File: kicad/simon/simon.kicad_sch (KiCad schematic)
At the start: 20 parts, among them J1 GPIO, J2 Power, U1 74LS06

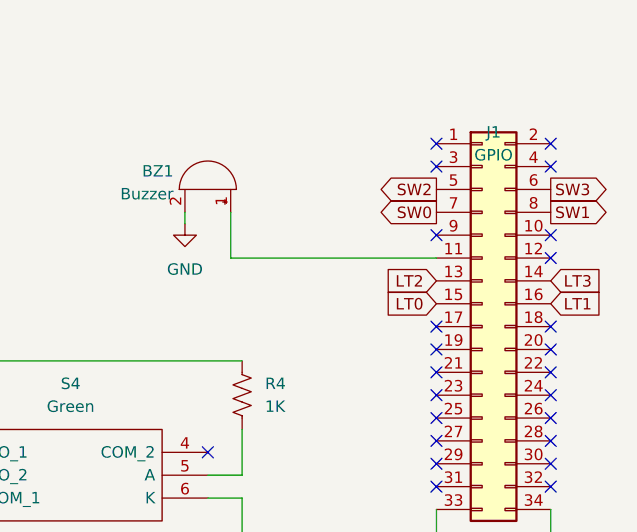
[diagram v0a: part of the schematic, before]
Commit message: Fixed trace routing to speaker.  This is the real production version.
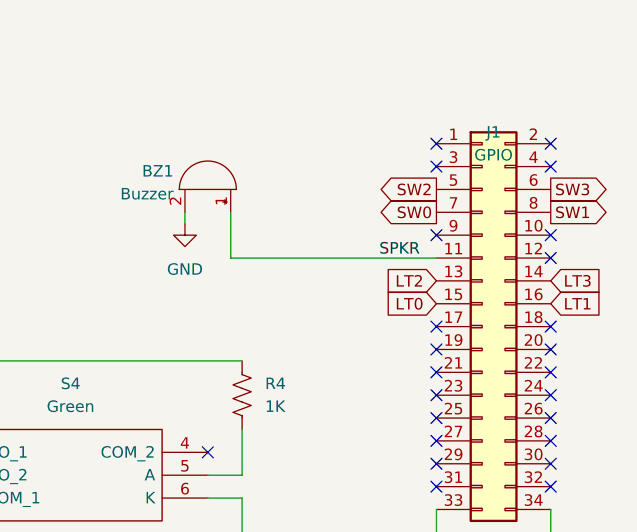
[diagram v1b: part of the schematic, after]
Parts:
- BZ1: footprint Buzzer_Beeper:Speaker_CUI_CMR-1206S-67 -> parts:XDCR_AT-1438-TWT-R
- S1, S2, S3, S4: footprint B3W9002Y1Y -> parts:B3W9002Y1Y
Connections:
- net SPKR: now reaches BZ1.1 (-), J1.11 (Pin_11)
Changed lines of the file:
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@@
     (stroke (width 0) (type default))
+  )
+  (label "SPKR" (at 201.93 46.99 0) (fields_autoplaced)
+    (effects (font (size 1.27 1.27)) (justify left bottom))
   )
   (global_label "LT0" (shape output) (at 49.53 95.25 180) (fields_autoplaced)
@@
       (effects (font (size 1.27 1.27)))
     )
-    (property "Footprint" "B3W9002Y1Y" (at 179.07 66.04 0)
+    (property "Footprint" "parts:B3W9002Y1Y" (at 179.07 66.04 0)
       (effects (font (size 1.27 1.27)) (justify left) hide)
     )
@@
       (effects (font (size 1.27 1.27)))
     )
-    (property "Footprint" "B3W9002Y1Y" (at 134.62 66.04 0)
+    (property "Footprint" "parts:B3W9002Y1Y" (at 134.62 66.04 0)
       (effects (font (size 1.27 1.27)) (justify left) hide)
     )
@@
       (effects (font (size 1.27 1.27)))
     )
-    (property "Footprint" "B3W9002Y1Y" (at 46.99 66.04 0)
+    (property "Footprint" "parts:B3W9002Y1Y" (at 46.99 66.04 0)
       (effects (font (size 1.27 1.27)) (justify left) hide)
     )
@@
       (effects (font (size 1.27 1.27)) (justify right))
     )
-    (property "Footprint" "Buzzer_Beeper:Speaker_CUI_CMR-1206S-67" (at 185.42 40.005 90)
+    (property "Footprint" "parts:XDCR_AT-1438-TWT-R" (at 185.42 40.005 90)
       (effects (font (size 1.27 1.27)) hide)
     )
@@
       (effects (font (size 1.27 1.27)))
     )
-    (property "Footprint" "B3W9002Y1Y" (at 91.44 66.04 0)
-      (effects (font (size 1.27 1.27)) (justify left) hide)
-    )
+    (property "Footprint" "parts:B3W9002Y1Y" (at 91.44 66.04 0)
+      (effects (font (size 1.27 1.27)) (justify left) hide)
+    )

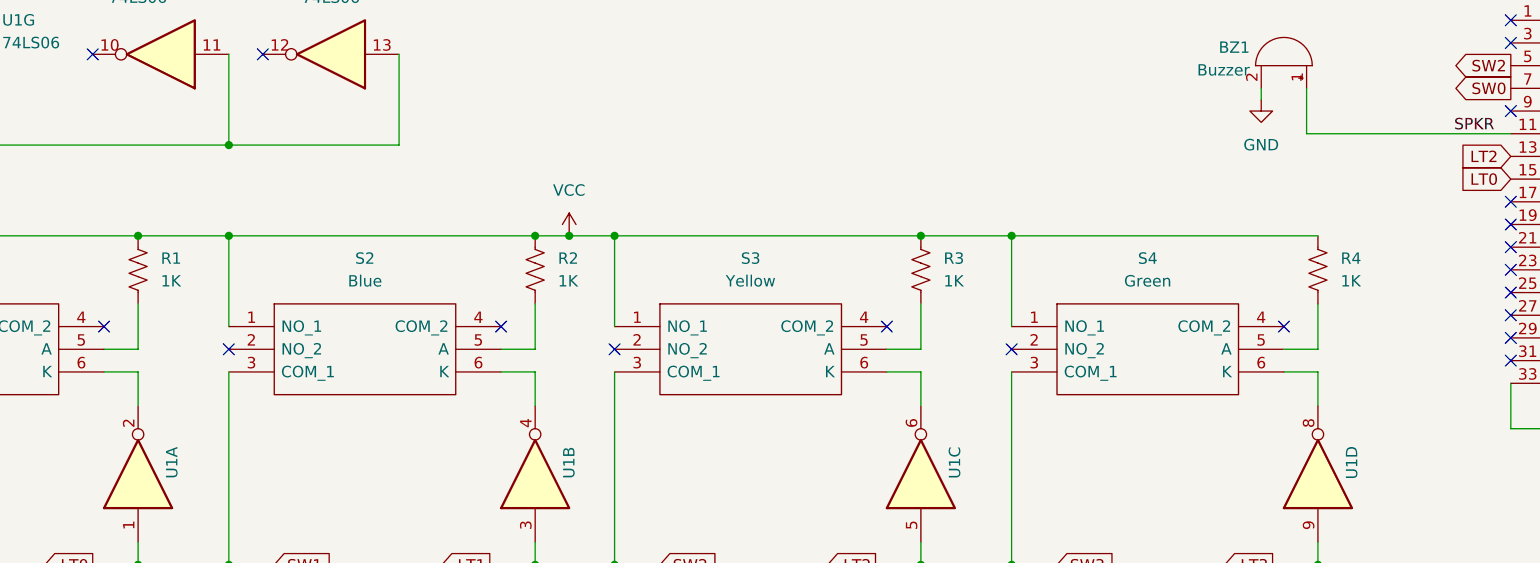
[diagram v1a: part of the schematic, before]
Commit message: Updated board with larger holes, BOM, and part numbers. This corresponds to the community shared version (v1.0.1)
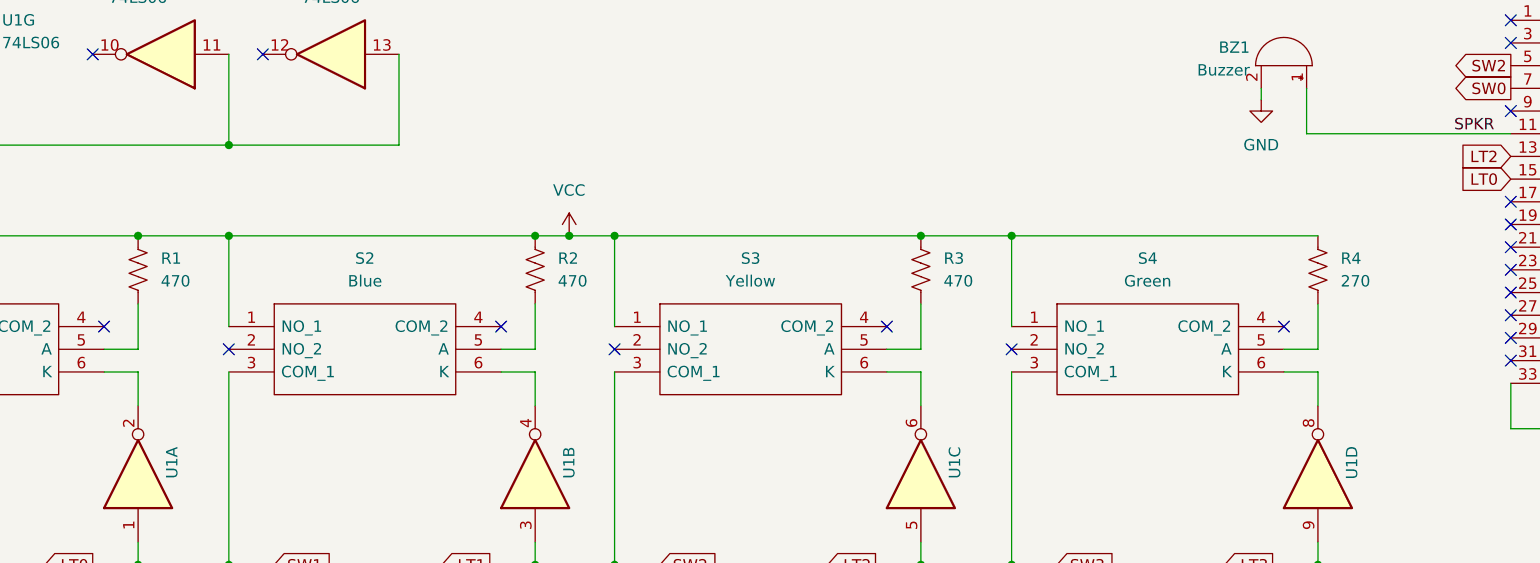
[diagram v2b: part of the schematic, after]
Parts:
- BZ1: Manufacturer_Name (none) -> PUI Audio; Manufacturer_Part_Number (none) -> AT-1438-TWT-R; Mouser Part Number (none) -> 665-AT-1438TWTR; Mouser Price/Stock (none) -> https://www.mouser.com/ProductDetail/PUI-Audio/AT-1438-TWT-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
- J1: Manufacturer_Name (none) -> TE Connectivity; Manufacturer_Part_Number (none) -> 1-534206-7; Mouser Part Number (none) -> 571-15342067; Mouser Price/Stock (none) -> https://www.mouser.com/ProductDetail/571-15342067
- J2: Manufacturer_Name (none) -> TE Connectivity; Manufacturer_Part_Number (none) -> 5-146282-2; Mouser Part Number (none) -> 571-5-146282-2; Mouser Price/Stock (none) -> https://www.mouser.com/ProductDetail/TE-Connectivity/5-1462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
- R1, R2, R3: value 1K -> 470; Manufacturer_Name (none) -> TE Connectivity; Manufacturer_Part_Number (none) -> CFR16J470R; Mouser Part Number (none) -> 279-CFR16J470R; Mouser Price/Stock (none) -> https://www.mouser.com/ProductDetail/TE-Connectivity-Holswo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
- R10, R11, R12, R5, R6, R7, R8, R9: Manufacturer_Name (none) -> TE Connectivity; Manufacturer_Part_Number (none) -> CFR16J10K; Mouser Part Number (none) -> 279-CFR16J10K; Mouser Price/Stock (none) -> https://www.mouser.com/ProductDetail/TE-Connectivity-Holswo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
- R4: value 1K -> 270; Manufacturer_Name (none) -> TE Connectivity; Manufacturer_Part_Number (none) -> CFR16J270R; Mouser Part Number (none) -> 279-CFR16J270R; Mouser Price/Stock (none) -> https://www.mouser.com/ProductDetail/TE-Connectivity-AMP/CF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
- U1: Manufacturer_Name (none) -> Texas Instruments; Manufacturer_Part_Number (none) -> SN74LS06N; Mouser Part Number (none) -> 595-SN74LS06N; Mouser Price/Stock (none) -> https://www.mouser.com/ProductDetail/Texas-Instruments/SN74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
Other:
- title: Simon for SDK-85 -> Disco Memory Game for SDK-85
